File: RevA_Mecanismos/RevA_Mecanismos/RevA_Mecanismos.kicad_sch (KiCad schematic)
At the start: 26 parts, among them J1 PROG, SW1 SW_Push, U1 STM32L431RCTx, Y1 16MHz

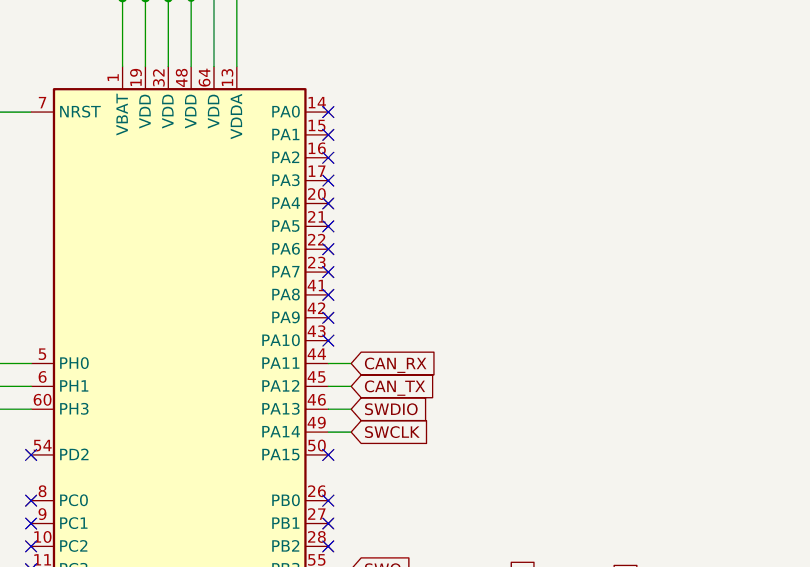
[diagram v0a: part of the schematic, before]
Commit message: Added H-Bridges and voltage regulators
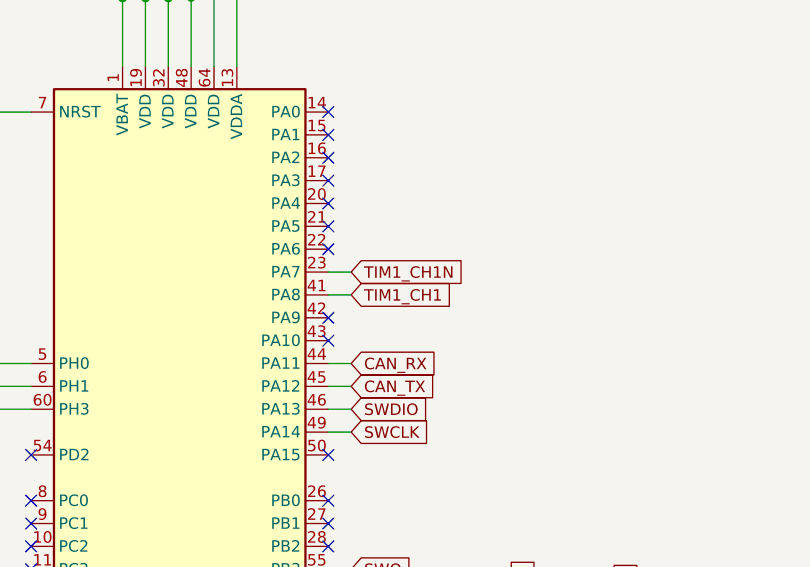
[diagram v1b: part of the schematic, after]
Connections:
- net TIM1_CH1N: now reaches U1.23 (PA7)
- net TIM1_CH1: now reaches U1.41 (PA8)
- no-connect marks 43 -> 41
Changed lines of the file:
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@@
   (no_connect (at 46.99 152.4))
   (no_connect (at 80.01 93.98))
-  (no_connect (at 80.01 106.68))
   (no_connect (at 46.99 157.48))
   (no_connect (at 46.99 170.18))
@@
   (no_connect (at 251.46 123.19))
   (no_connect (at 67.31 175.26))
-  (no_connect (at 80.01 109.22))
   (no_connect (at 80.01 91.44))
   (no_connect (at 46.99 149.86))
@@
     (stroke (width 0) (type solid))
   )
+  (wire (pts (xy 80.01 109.22) (xy 82.55 109.22))
+    (stroke (width 0) (type default))
+  )
   (wire (pts (xy 64.77 176.53) (xy 62.23 176.53))
     (stroke (width 0) (type solid))
@@
   (wire (pts (xy 43.18 116.84) (xy 46.99 116.84))
     (stroke (width 0) (type solid))
+  )
+  (wire (pts (xy 80.01 106.68) (xy 82.55 106.68))
+    (stroke (width 0) (type default))
   )
   (wire (pts (xy 228.6 76.2) (xy 232.41 76.2))
@@
     )
   )
+  (global_label "TIM1_CH1N" (shape input) (at 82.55 106.68 0)
+    (effects (font (size 1.27 1.27)) (justify left))
+    (property "Intersheetrefs" "${INTERSHEET_REFS}" (at 93.6233 106.7594 0)
+      (effects (font (size 1.27 1.27)) (justify left) hide)
+    )
+  )
   (global_label "SWDIO" (shape input) (at 252.73 118.11 0)
     (effects (font (size 1.27 1.27)) (justify left))
@@
     )
   )
+  (global_label "TIM1_CH1" (shape input) (at 82.55 109.22 0)
+    (effects (font (size 1.27 1.27)) (justify left))
+    (property "Intersheetrefs" "${INTERSHEET_REFS}" (at 93.6233 109.2994 0)
+      (effects (font (size 1.27 1.27)) (justify left) hide)
+    )
+  )

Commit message: Created PCB project
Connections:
- net +3.3V: now also R2.2; no longer R2.1
- net GND: now also C12.2, SW1.2; no longer C12.1, SW1.1
- net NRST: now also C12.1, SW1.1; no longer C12.2, SW1.2
- net SCL: now also R2.1; no longer R2.2
- net IO_1: now reaches U1.14 (PA0)
- net IO_2: now reaches U1.15 (PA1)
- net IO_3: now reaches U1.16 (PA2)
- net IO_4: now reaches U1.17 (PA3)
- net IO_5: now reaches U1.20 (PA4)
- net IO_6: now reaches U1.21 (PA5)
- no-connect marks 41 -> 35
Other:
- added sheet IO (io.kicad_sch)
- moved on the sheet: C1, C10, C11, C12, C2, C3, C4, C5, C6, C7, C8, C9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

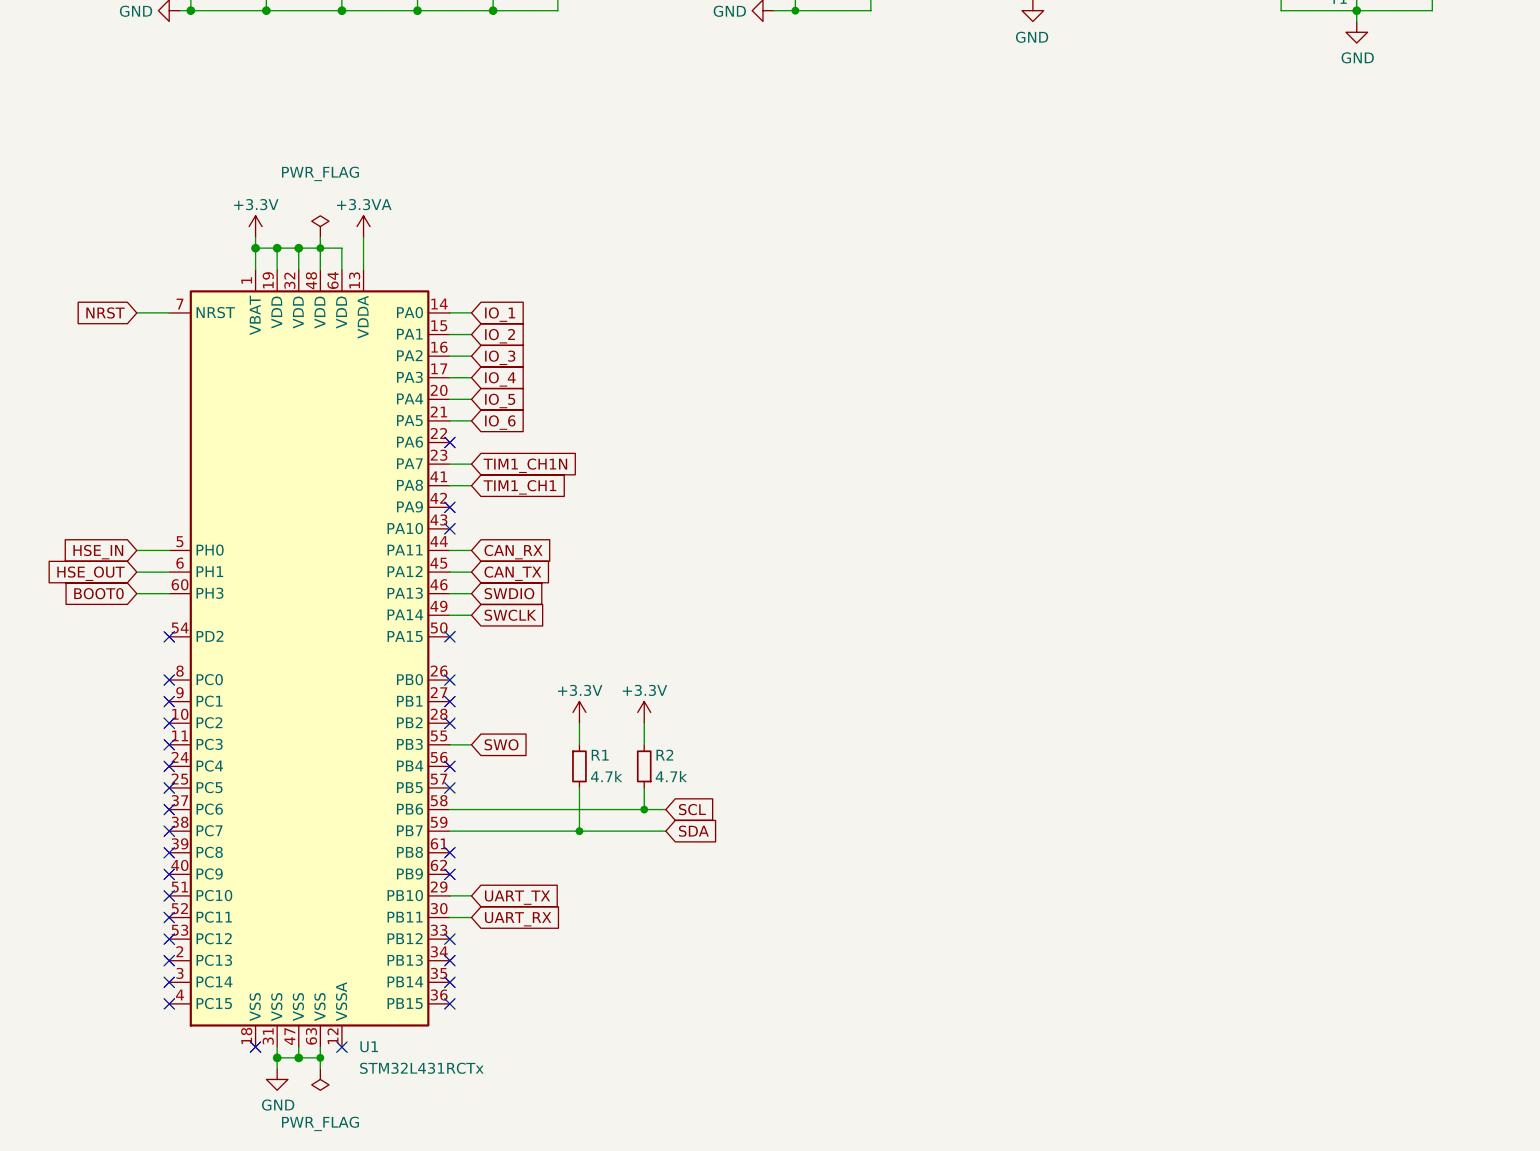
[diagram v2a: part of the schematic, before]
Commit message: Adiciones a secciones de motores y power supply para placa de mecanismos
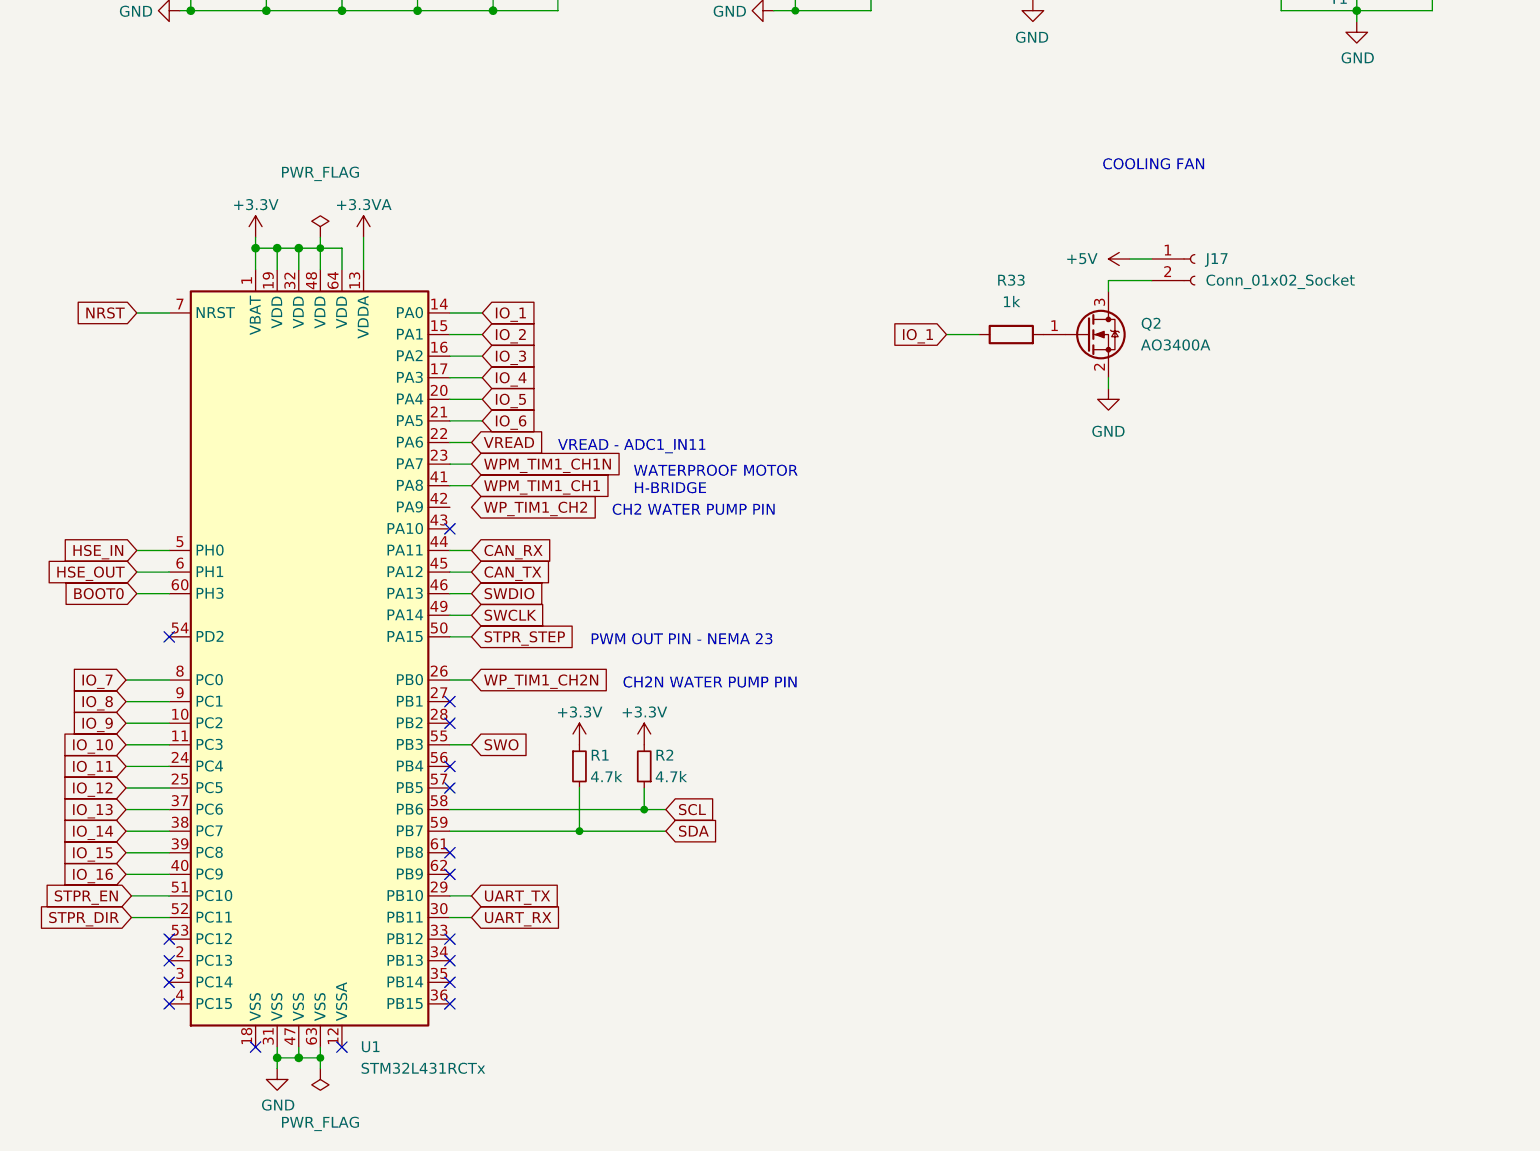
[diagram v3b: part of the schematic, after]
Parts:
- added J17: Conn_01x02_Socket, Connector_PinHeader_2.54mm:PinHeader_1x02_P2.54mm_Vertical, symbol Connector:Conn_01x02_Socket
- added Q2: AO3400A, Package_TO_SOT_SMD:SOT-23, symbol Transistor_FET:AO3400A
- added R33: 1k, symbol Device:R
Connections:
- net GND: now also Q2.2 (S)
- net IO_1: now also R33.1
- net IO_9: now reaches U1.10 (PC2)
- net IO_10: now reaches U1.11 (PC3)
- net VREAD: now reaches U1.22 (PA6)
- net IO_11: now reaches U1.24 (PC4)
- net IO_12: now reaches U1.25 (PC5)
- net WP_TIM1_CH2N: now reaches U1.26 (PB0)
- net IO_13: now reaches U1.37 (PC6)
- net IO_14: now reaches U1.38 (PC7)
- net IO_15: now reaches U1.39 (PC8)
- net IO_16: now reaches U1.40 (PC9)
- net STPR_STEP: now reaches U1.50 (PA15)
- net STPR_EN: now reaches U1.51 (PC10)
- net STPR_DIR: now reaches U1.52 (PC11)
- net IO_7: now reaches U1.8 (PC0)
- net IO_8: now reaches U1.9 (PC1)
- net TIM1_CH1 renamed WPM_TIM1_CH1
- net TIM1_CH1N renamed WPM_TIM1_CH1N
- new net: Q2.1 (G), R33.2
- new net: J17.2 (Pin_2), Q2.3 (D)
- new net +5V: J17.1 (Pin_1)
- no-connect marks 35 -> 19
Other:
- note added: "CH2 WATER PUMP PIN"
- note added: "CH2N WATER PUMP PIN"
- note added: "COOLING FAN"
- note added: "PWM OUT PIN - NEMA 23"
- note added: "VREAD - ADC1_IN11"
- note added: "WATERPROOF MOTOR H-BRIDGE"

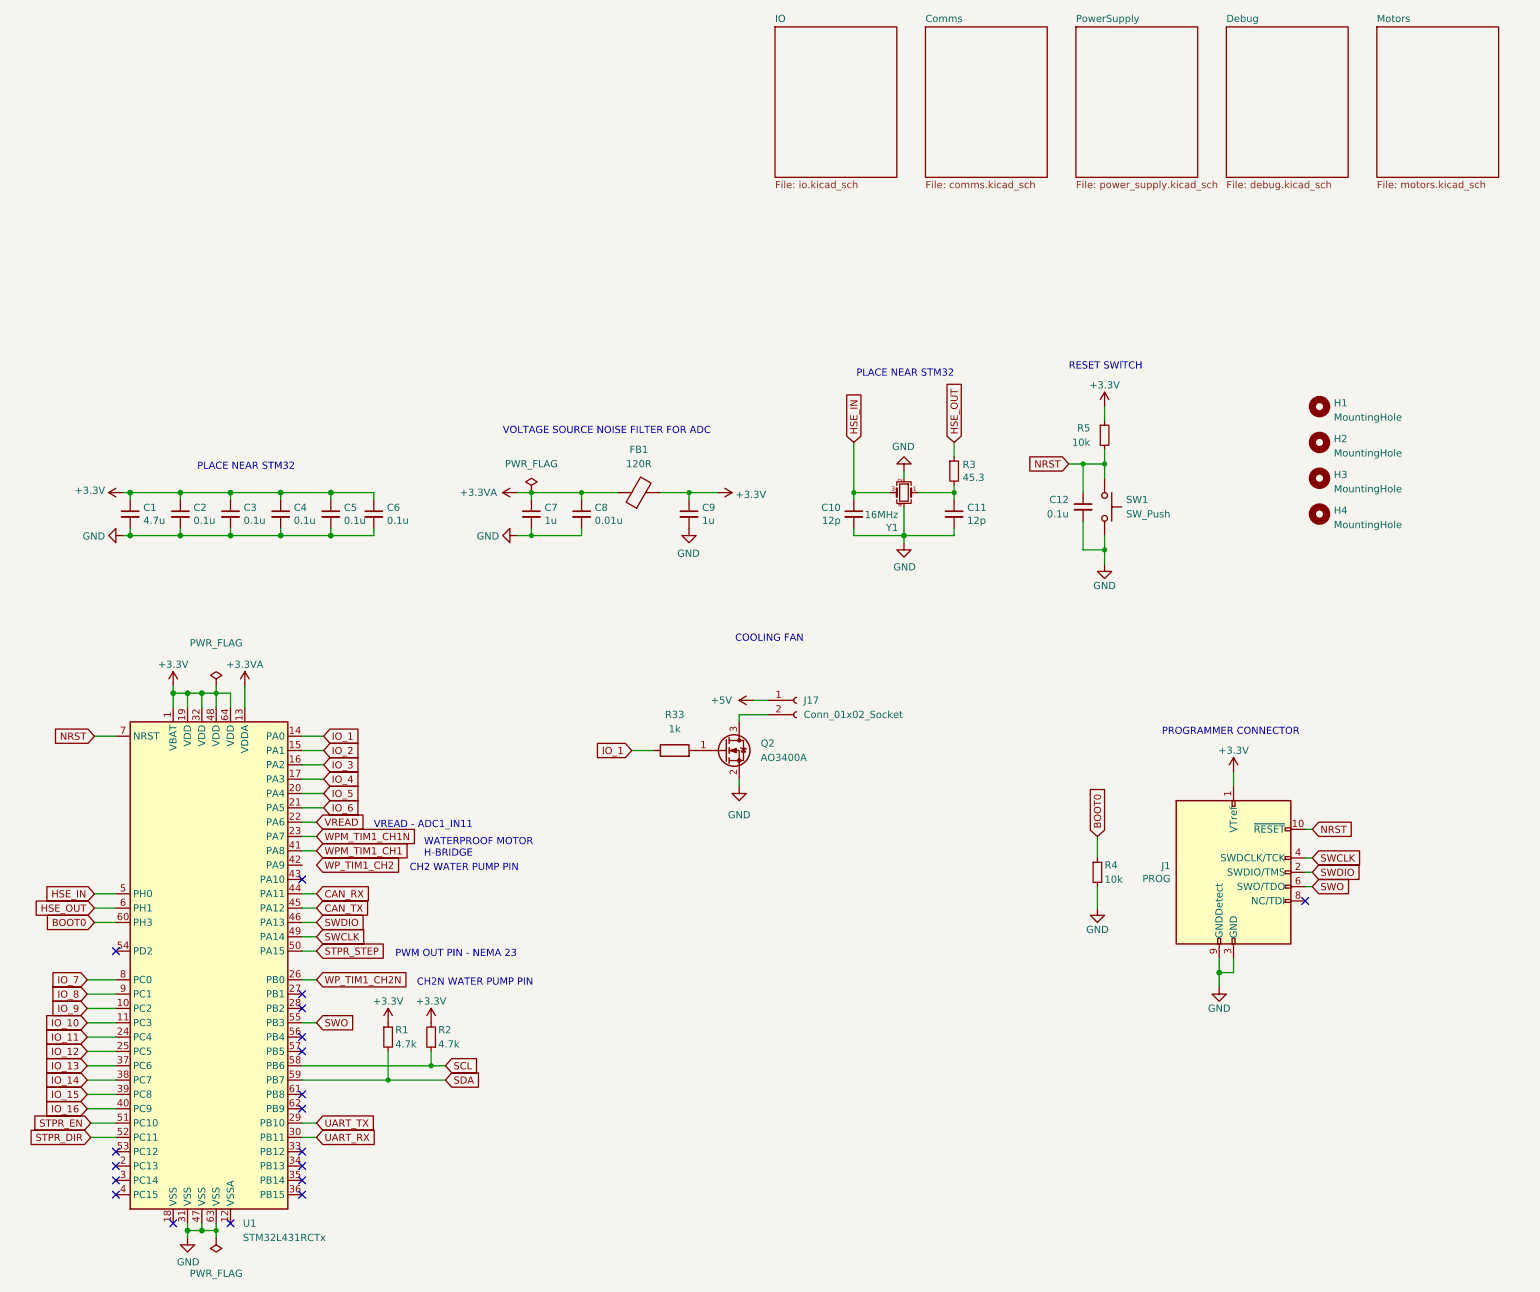
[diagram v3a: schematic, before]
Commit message: Debug connectors and pwr flag to +12v
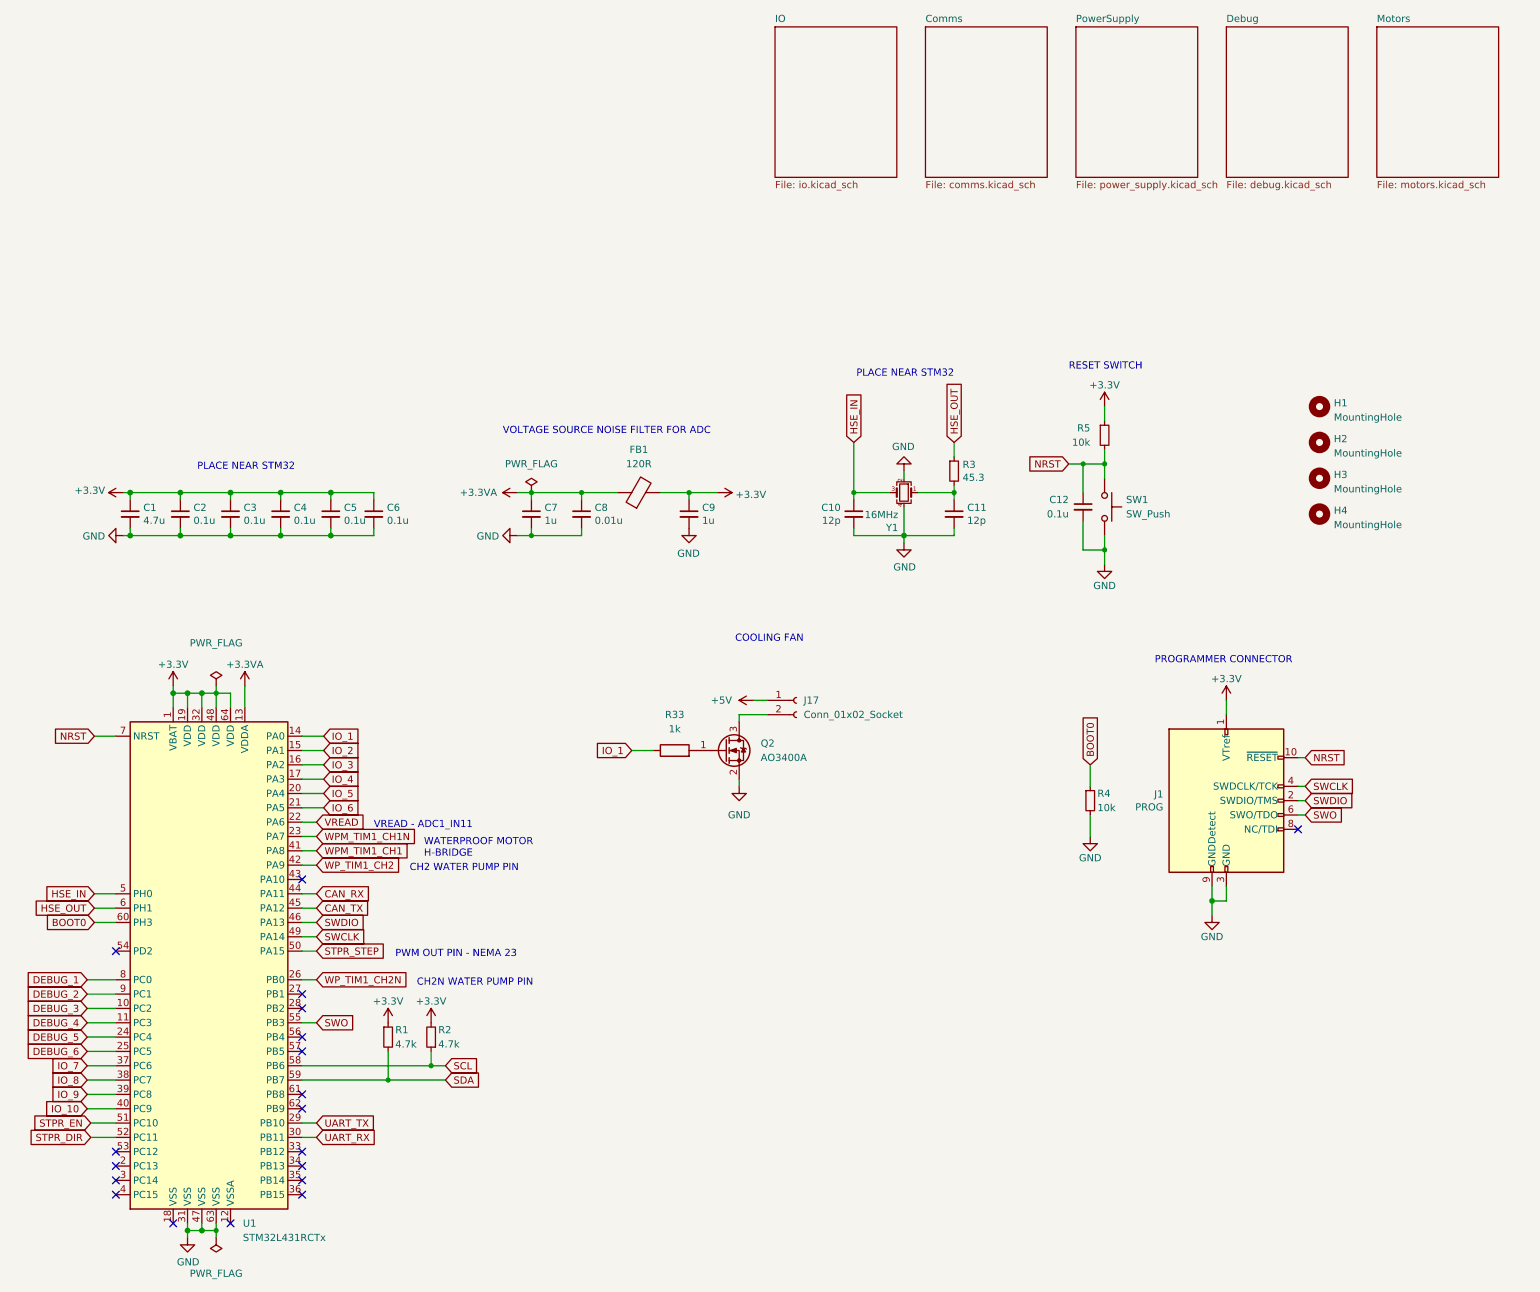
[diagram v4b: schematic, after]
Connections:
- net IO_13 is gone; now on net IO_7: U1.37 (PC6)
- net IO_14 is gone; now on net IO_8: U1.38 (PC7)
- net IO_15 is gone; now on net IO_9: U1.39 (PC8)
- net IO_16 is gone; now on net IO_10: U1.40 (PC9)
- net IO_10: no longer U1.11 (PC3)
- net IO_7: no longer U1.8 (PC0)
- net IO_8: no longer U1.9 (PC1)
- net IO_9: no longer U1.10 (PC2)
- net WP_TIM1_CH2: now also U1.42 (PA9)
- net IO_11 renamed DEBUG_5
- net IO_12 renamed DEBUG_6
- new net DEBUG_1: U1.8 (PC0)
- new net DEBUG_2: U1.9 (PC1)
- new net DEBUG_3: U1.10 (PC2)
- new net DEBUG_4: U1.11 (PC3)
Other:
- moved on the sheet: J1, R4
